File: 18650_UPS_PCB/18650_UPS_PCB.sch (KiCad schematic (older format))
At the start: 21 parts, among them J1 USB_B_Micro, J2 Conn_02x04_Odd_Even, SW2 ALPSALPINE_SKRHADE011, U1 STLINK-V3MINI, U7 INA219AxD, U8 SSD1306_128_32, U9 STM32F030F4Px

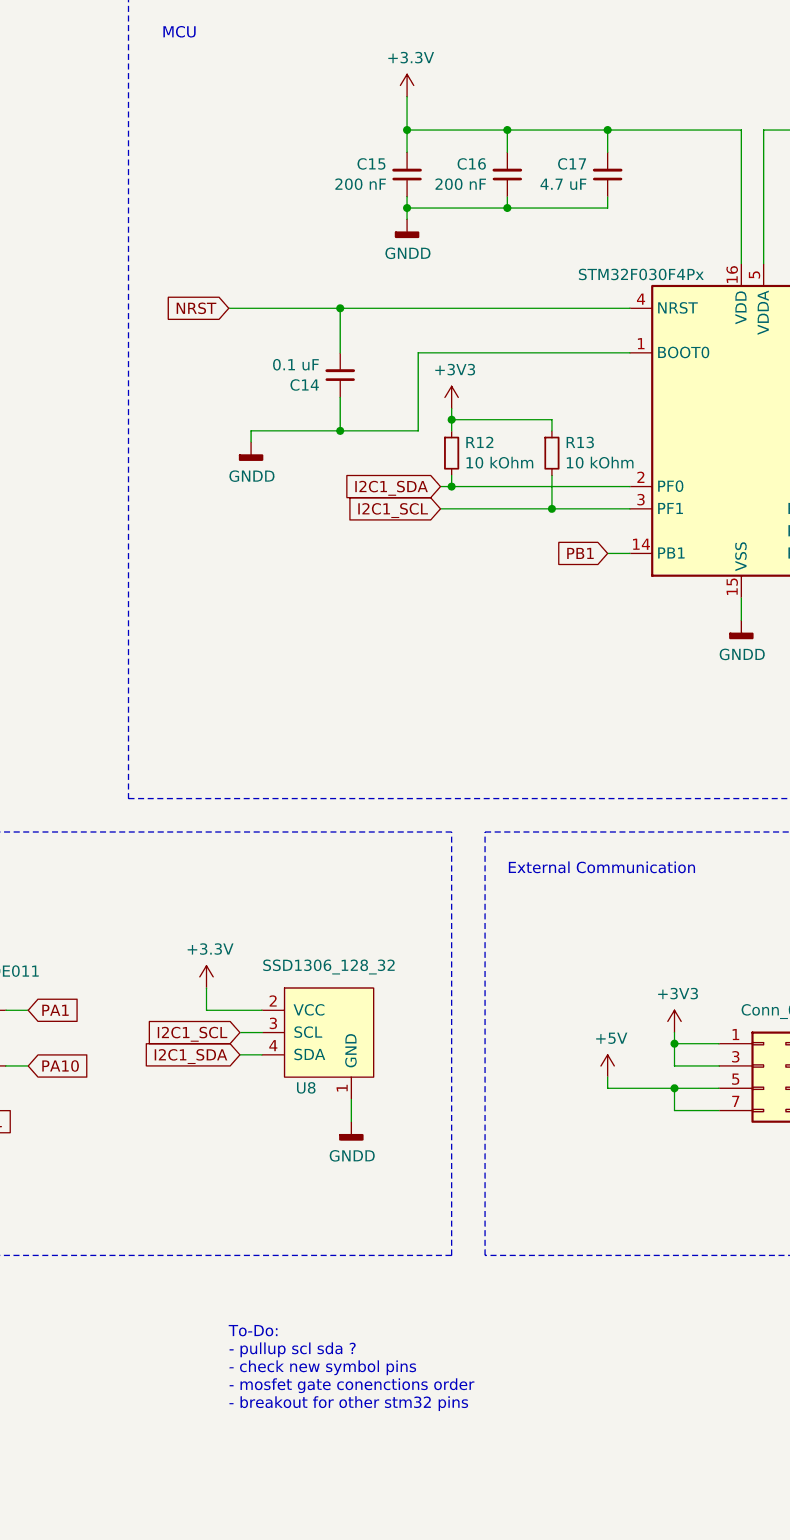
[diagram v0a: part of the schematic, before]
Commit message: changed resistor values tps63000
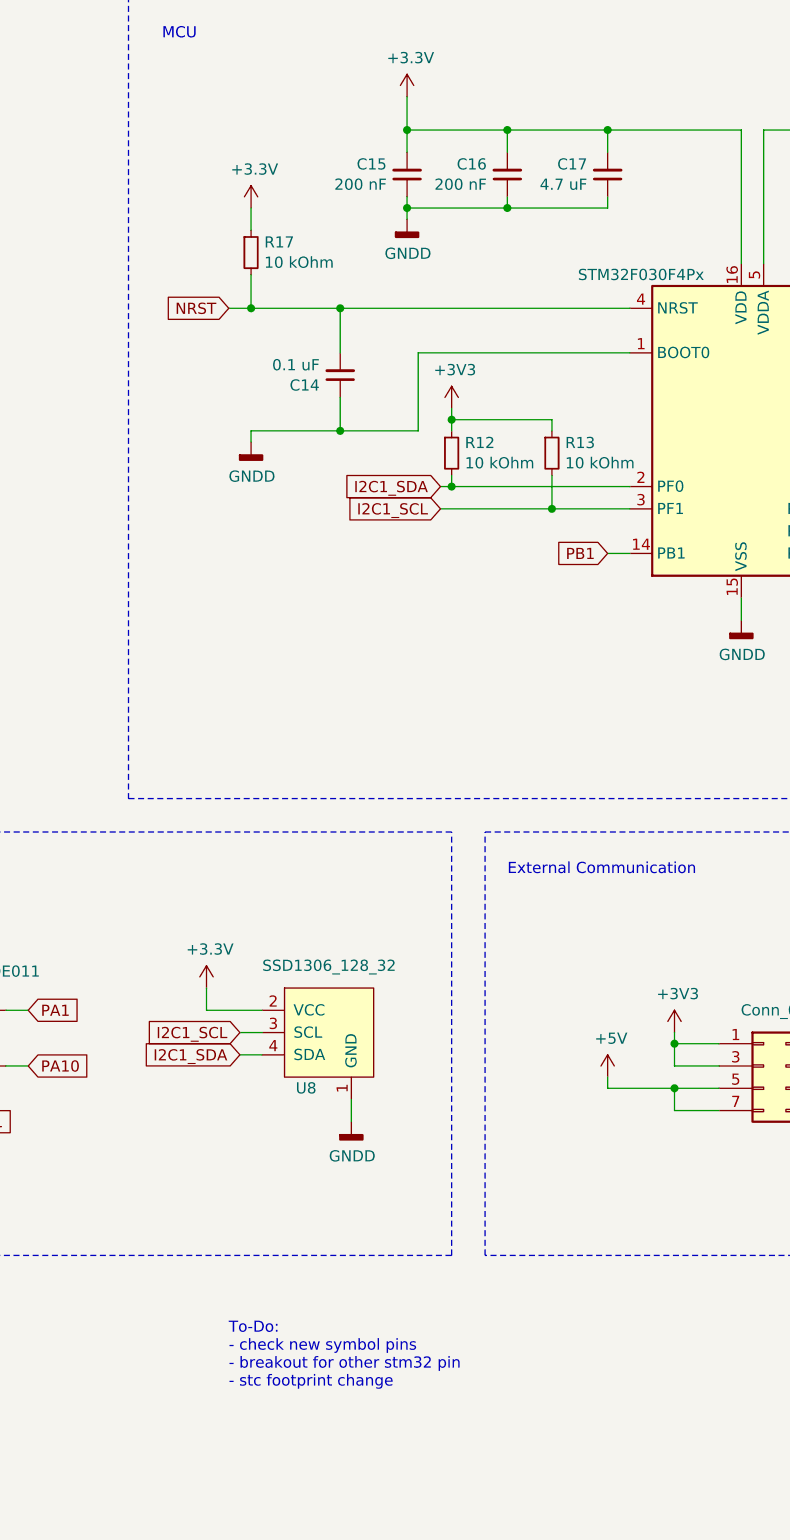
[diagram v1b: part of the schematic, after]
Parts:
- added R17: 10 kOhm, Resistor_SMD:R_0603_1608Metric, symbol Device:R_Small
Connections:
- net +3V3: now also R17.1
- net NRST: now also R17.2
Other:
- note added: "To-Do:\n- check new symbol pins\n- breakout for other stm32 pin\n- stc footprint change"
- note removed: "To-Do:\n- pullup scl sda ?\n- check new symbol pins\n- mosfet gate conenctions order\n- breakout for other stm32 pins"
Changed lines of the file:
@@
 Comment4 ""
 $EndDescr
-Text Notes 7100 7050 0    50   ~ 0
-To-Do:\n- pullup scl sda ?\n- check new symbol pins\n- mosfet gate conenctions order\n- breakout for other stm32 pins
+Text Notes 7100 6950 0    50   ~ 0
+To-Do:\n- check new symbol pins\n- breakout for other stm32 pin\n- stc footprint change
 Text Notes 2900 950  0    50   ~ 0
 STLINK
@@
 	9900 3000 10000 3000
 Wire Wire Line
-	7100 2100 7600 2100
+	7100 2100 7200 2100
 Wire Wire Line
 	3000 6500 3300 6500
@@
 Wire Wire Line
 	10000 2700 9900 2700
+$Comp
+L Device:R_Small R?
+U 1 1 60AC88F6
+P 7200 1850
+AR Path="/609F1585/60AC88F6" Ref="R?"  Part="1"
+AR Path="/60AC88F6" Ref="R17"  Part="1"
+F 0 "R17" H 7259 1896 50  0000 L CNN
+F 1 "10 kOhm" H 7259 1805 50  0000 L CNN
+F 2 "Resistor_SMD:R_0603_1608Metric" H 7200 1850 50  0001 C CNN
+F 3 "~" H 7200 1850 50  0001 C CNN
+	1    7200 1850
+	1    0    0    -1
+$EndComp
+Wire Wire Line
+	7200 2100 7200 1950
+Connection ~ 7200 2100
+Wire Wire Line
+	7200 2100 7600 2100
+$Comp
+L power:+3.3V #PWR020
+U 1 1 60ADE6A0
+P 7200 1650
+AR Path="/60ADE6A0" Ref="#PWR020"  Part="1"
+AR Path="/609F1585/60ADE6A0" Ref="#PWR?"  Part="1"
+F 0 "#PWR020" H 7200 1500 50  0001 C CNN
+F 1 "+3.3V" H 7215 1823 50  0000 C CNN
+F 2 "" H 7200 1650 50  0001 C CNN
+F 3 "" H 7200 1650 50  0001 C CNN
+	1    7200 1650
+	1    0    0    -1
+$EndComp
+Wire Wire Line
+	7200 1750 7200 1650
 $EndSCHEMATC

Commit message: ordered
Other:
- note removed: "To-Do:\n- check new symbol pins\n- breakout for other stm32 pin\n- stc footprint change"
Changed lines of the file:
@@
 Comment4 ""
 $EndDescr
-Text Notes 7100 6950 0    50   ~ 0
-To-Do:\n- check new symbol pins\n- breakout for other stm32 pin\n- stc footprint change
 Text Notes 2900 950  0    50   ~ 0
 STLINK

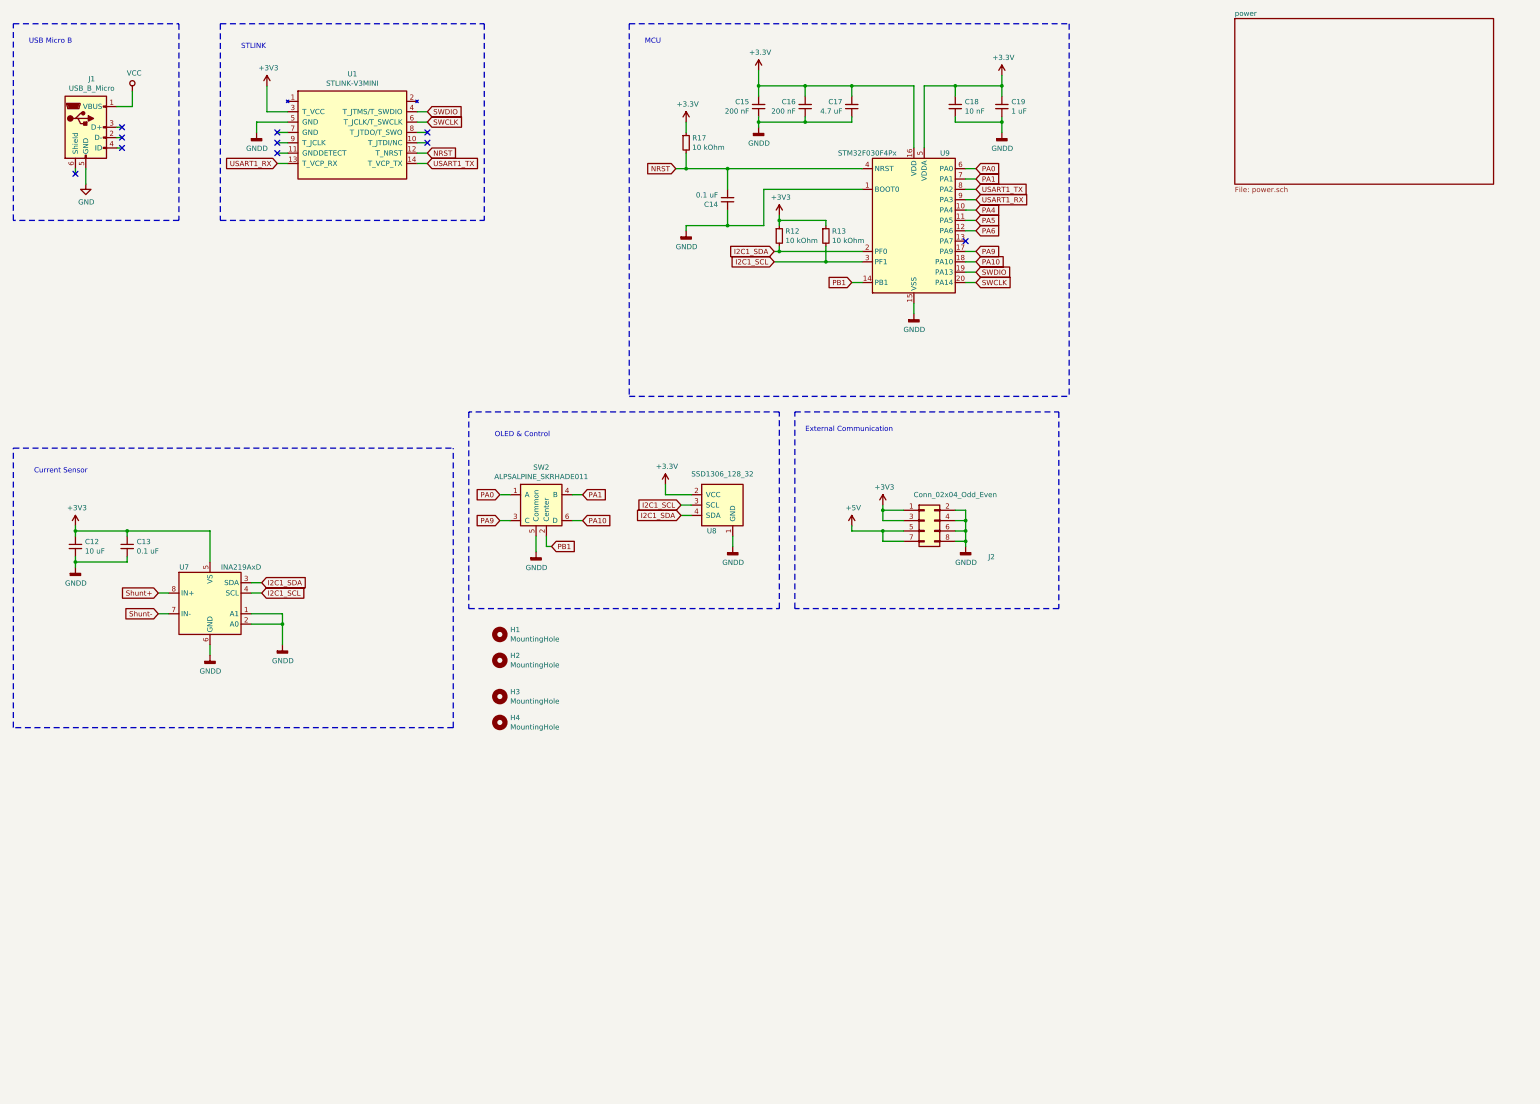
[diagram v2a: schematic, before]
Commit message: v2 layout started
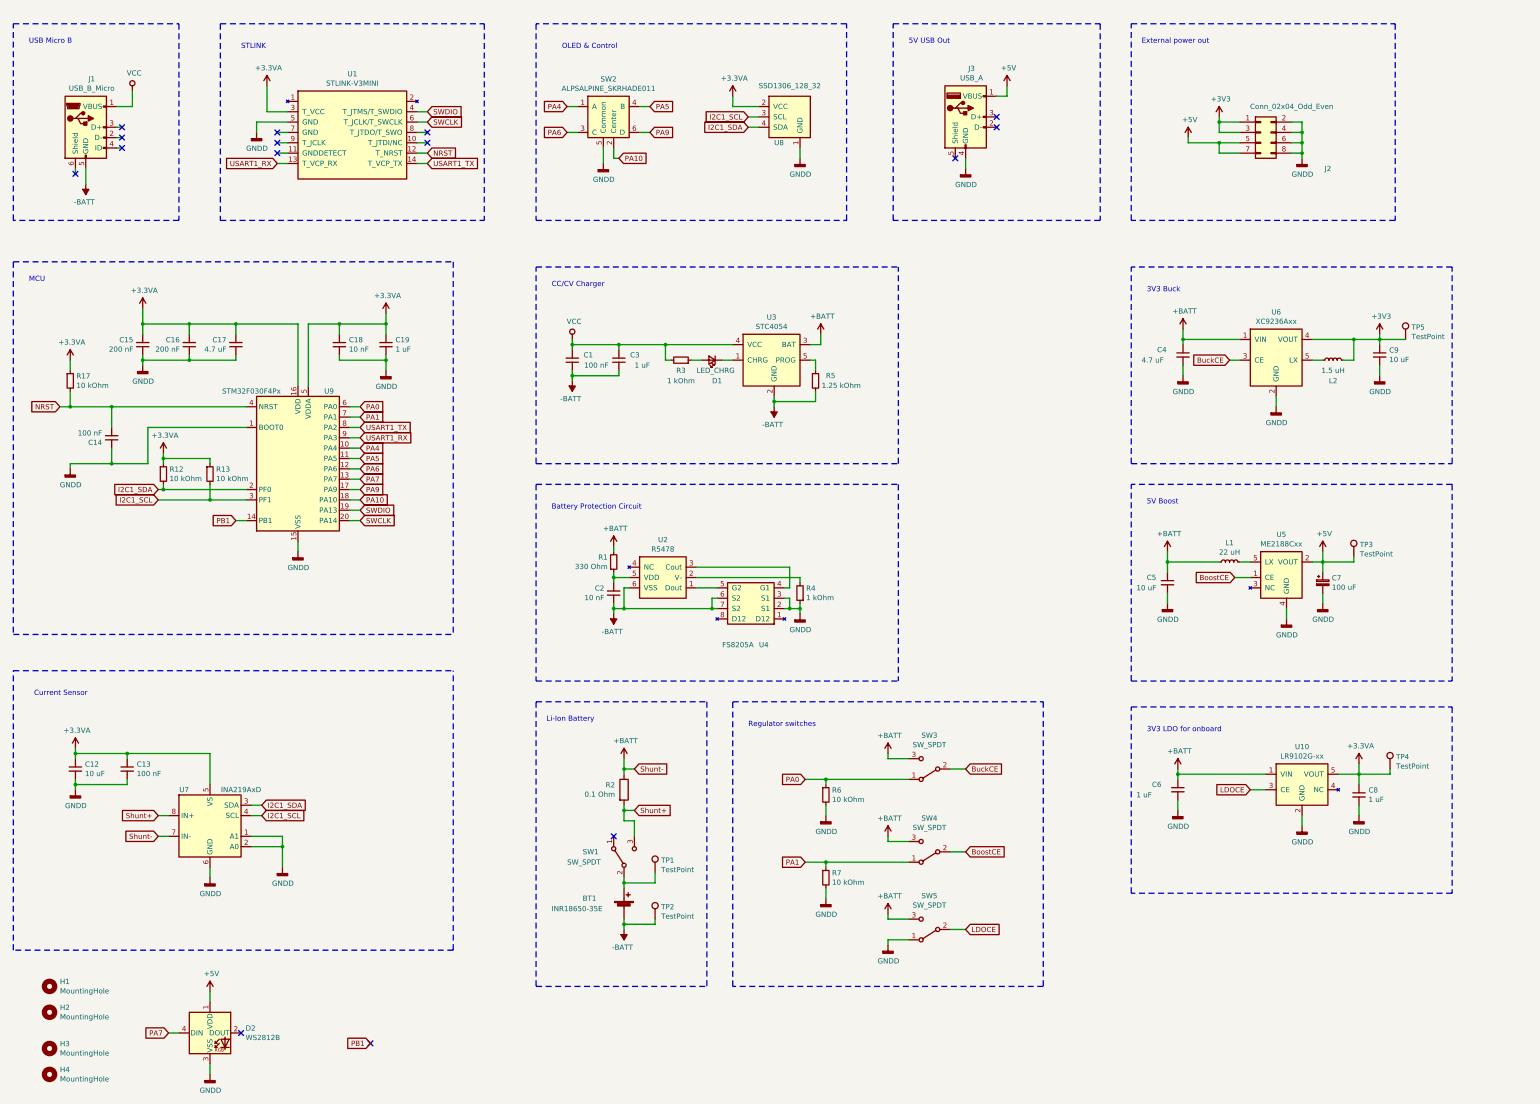
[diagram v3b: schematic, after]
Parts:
- added BT1: INR18650-35E, Battery:BatteryHolder_Keystone_1042_1x18650, symbol Device:Battery_Cell
- added C1: 100 nF, Capacitor_SMD:C_0603_1608Metric, symbol Device:C_Small
- added C2: 10 nF, Capacitor_SMD:C_0603_1608Metric, symbol Device:C_Small
- added C3: 1 uF, Capacitor_SMD:C_0603_1608Metric, symbol Device:C_Small
- added C4: 4.7 uF, Capacitor_SMD:C_0805_2012Metric, symbol Device:C_Small
- added C5, C9: 10 uF, Capacitor_SMD:C_0805_2012Metric, symbol Device:C_Small
- added C6, C8: 1 uF, Capacitor_SMD:C_0805_2012Metric, symbol Device:C_Small
- added C7: 100 uF, Capacitor_SMD:CP_Elec_5x5.4, symbol Device:CP_Small
- added D1: LED_CHRG, LED_SMD:LED_0603_1608Metric, symbol Device:LED_Small
- added D2: WS2812B, LED_SMD:LED_WS2812B_PLCC4_5.0x5.0mm_P3.2mm, symbol LED:WS2812B
- added J3: USB_A, Connector_USB:USB_A_CNCTech_1001-011-01101_Horizontal, symbol Connector:USB_A
- added L1: 22 uH, Inductor_SMD:L_Bourns-SRN6028, symbol Device:L_Small
- added L2: 1.5 uH, Inductor_SMD:L_Taiyo-Yuden_MD-4040, symbol Device:L_Small
- added R1: 330 Ohm, Resistor_SMD:R_0603_1608Metric, symbol Device:R_Small
- added R2: 0.1 Ohm, Resistor_SMD:R_2512_6332Metric, symbol Device:R
- added R3, R4: 1 kOhm, Resistor_SMD:R_0603_1608Metric, symbol Device:R_Small
- added R5: 1.25 kOhm, Resistor_SMD:R_0603_1608Metric, symbol Device:R_Small
- added R6, R7: 10 kOhm, Resistor_SMD:R_0603_1608Metric, symbol Device:R_Small
- added SW1: SW_SPDT, CUSTOM_FOOTPRINTS:ALPS_SPEF210101, symbol Switch:SW_SPDT
- added SW3, SW4, SW5: SW_SPDT, Button_Switch_SMD:SW_SPDT_PCM12, symbol Switch:SW_SPDT
- added TP1, TP2, TP3, TP4, TP5: TestPoint, TestPoint:TestPoint_Keystone_5015_Micro-Minature, symbol Connector:TestPoint
- added U10: LR9102G-xx, Package_TO_SOT_SMD:SOT-353_SC-70-5, symbol CUSTOM_PARTS:LR9102G-xx
- added U2: R5478, Package_TO_SOT_SMD:SOT-23-6, symbol CUSTOM_PARTS:R5478
- added U3: STC4054, Package_TO_SOT_SMD:TSOT-23-5, symbol CUSTOM_PARTS:STC4054
- added U4: FS8205A, Package_SO:TSSOP-8_4.4x3mm_P0.65mm, symbol CUSTOM_PARTS:FS8205A
- added U5: ME2188Cxx, Package_TO_SOT_SMD:SOT-23-5, symbol CUSTOM_PARTS:ME2188Cxx
- added U6: XC9236Axx, Package_TO_SOT_SMD:SOT-23-5, symbol CUSTOM_PARTS:XC9236Axx
- C13, C14: value 0.1 uF -> 100 nF
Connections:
- net +3V3: now also C9.1, L2.2, TP5.1, U6.4 (VOUT); no longer C12.1, C13.1, C15.2, C16.2, C17.2, C18.1, C19.1, R12.1, R13.1, R17.1, U1.3 (T_VCC), U7.5 (VS), U8.2 (VCC), U9.16 (VDD), U9.5 (VDDA)
- net +5V: now also C7.1, D2.1 (VDD), J3.1 (VBUS), TP3.1, U5.2 (VOUT)
- net GNDD: now also C4.2, C5.2, C6.2, C7.2, C8.2, C9.2, D2.3 (VSS), J3.4 (GND), R4.1, R6.2, R7.2, SW5.1 (A), U10.2 (GND), U4.2 (S1), U4.3 (S1), U5.4 (GND), U6.2 (GND)
- net PA0: now also R6.1, SW3.1 (A); no longer SW2.1 (A)
- net PA1: now also R7.1, SW4.1 (A); no longer SW2.4 (B)
- net PA10: now also SW2.2 (Center); no longer SW2.6 (D)
- net PA4: now also SW2.1 (A)
- net PA5: now also SW2.4 (B)
- net PA6: now also SW2.3 (C)
- net PA9: now also SW2.6 (D); no longer SW2.3 (C)
- net PB1: no longer SW2.2 (Center)
- net Shunt+: now also R2.2, SW1.3 (C)
- net VCC: now also C1.2, C3.2, R3.2, U3.4 (VCC)
- net PA7: now reaches U9.13 (PA7)
- net PA7: now also D2.4 (DIN)
- net GND renamed -BATT
- net -BATT: now also BT1.2 (-), C1.1, C2.1, C3.1, R5.2, TP2.1, U2.6 (VSS), U3.2 (GND), U4.6 (S2), U4.7 (S2)
- net Shunt- renamed +BATT
- net +BATT: now also C4.1, C5.1, C6.1, L1.1, R1.2, R2.1, SW3.3 (C), SW4.3 (C), SW5.3 (C), U10.1 (VIN), U3.3 (BAT), U6.1 (VIN)
- new net: BT1.1 (+), SW1.2 (B), TP1.1
- new net: U2.3 (Cout), U4.4 (G1)
- new net: U2.1 (Dout), U4.5 (G2)
- new net: R4.2, U2.2 (V-)
- new net: C2.2, R1.1, U2.5 (VDD)
- new net: R5.1, U3.5 (PROG)
- new net: D1.2 (A), R3.1
- new net: D1.1 (K), U3.1 (CHRG)
- new net: L2.1, U6.5 (LX)
- new net: L1.2, U5.5 (LX)
- new net +3.3VA: C12.1, C13.1, C15.2, C16.2, C17.2, C18.1, C19.1, C8.1, R12.1, R13.1, R17.1, TP4.1, U1.3 (T_VCC), U10.5 (VOUT), U7.5 (VS), U8.2 (VCC), U9.16 (VDD), U9.5 (VDDA)
- new net BoostCE: SW4.2 (B), U5.1 (CE)
- new net BuckCE: SW3.2 (B), U6.3 (CE)
- new net LDOCE: SW5.2 (B), U10.3 (CE)
- no-connect marks 10 -> 15
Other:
- note added: "3V3 Buck"
- note added: "3V3 LDO for onboard"
- note added: "5V Boost"
- note added: "5V USB Out"
- note added: "Battery Protection Circuit"
- note added: "CC/CV Charger"
- note added: "External power out"
- note added: "Li-Ion Battery"
- note added: "Regulator switches"
- note removed: "External Communication"
- moved on the sheet: C12, C13, C14, C15, C16, C17, C18, C19, H1, H2, H3, H4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
